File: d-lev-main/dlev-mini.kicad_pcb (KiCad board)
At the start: 4 copper layers, 175.3 x 163.3 mm, 126 parts, among them J1 S12B-PH-SM4-TB, J2 Tag-Connect TC2030-NL, J3 S8B-PH-SM4-TB, J4 S8B-PH-SM4-TB, J5 S6B-PH-SM4-TB, Q1 BSS138, Q2 BSS138, Q3 BSS138, Q4 BSS138, Q5 BSS138, SW1 RotaryEncoder_Switch, SW2 RotaryEncoder_Switch, SW3 RotaryEncoder_Switch, SW4 RotaryEncoder_Switch, SW5 RotaryEncoder_Switch, SW6 RotaryEncoder_Switch, SW7 RotaryEncoder_Switch, SW8 RotaryEncoder_Switch, U2 25LCxxx, U3 AC608, U4 AMS1117-3.3

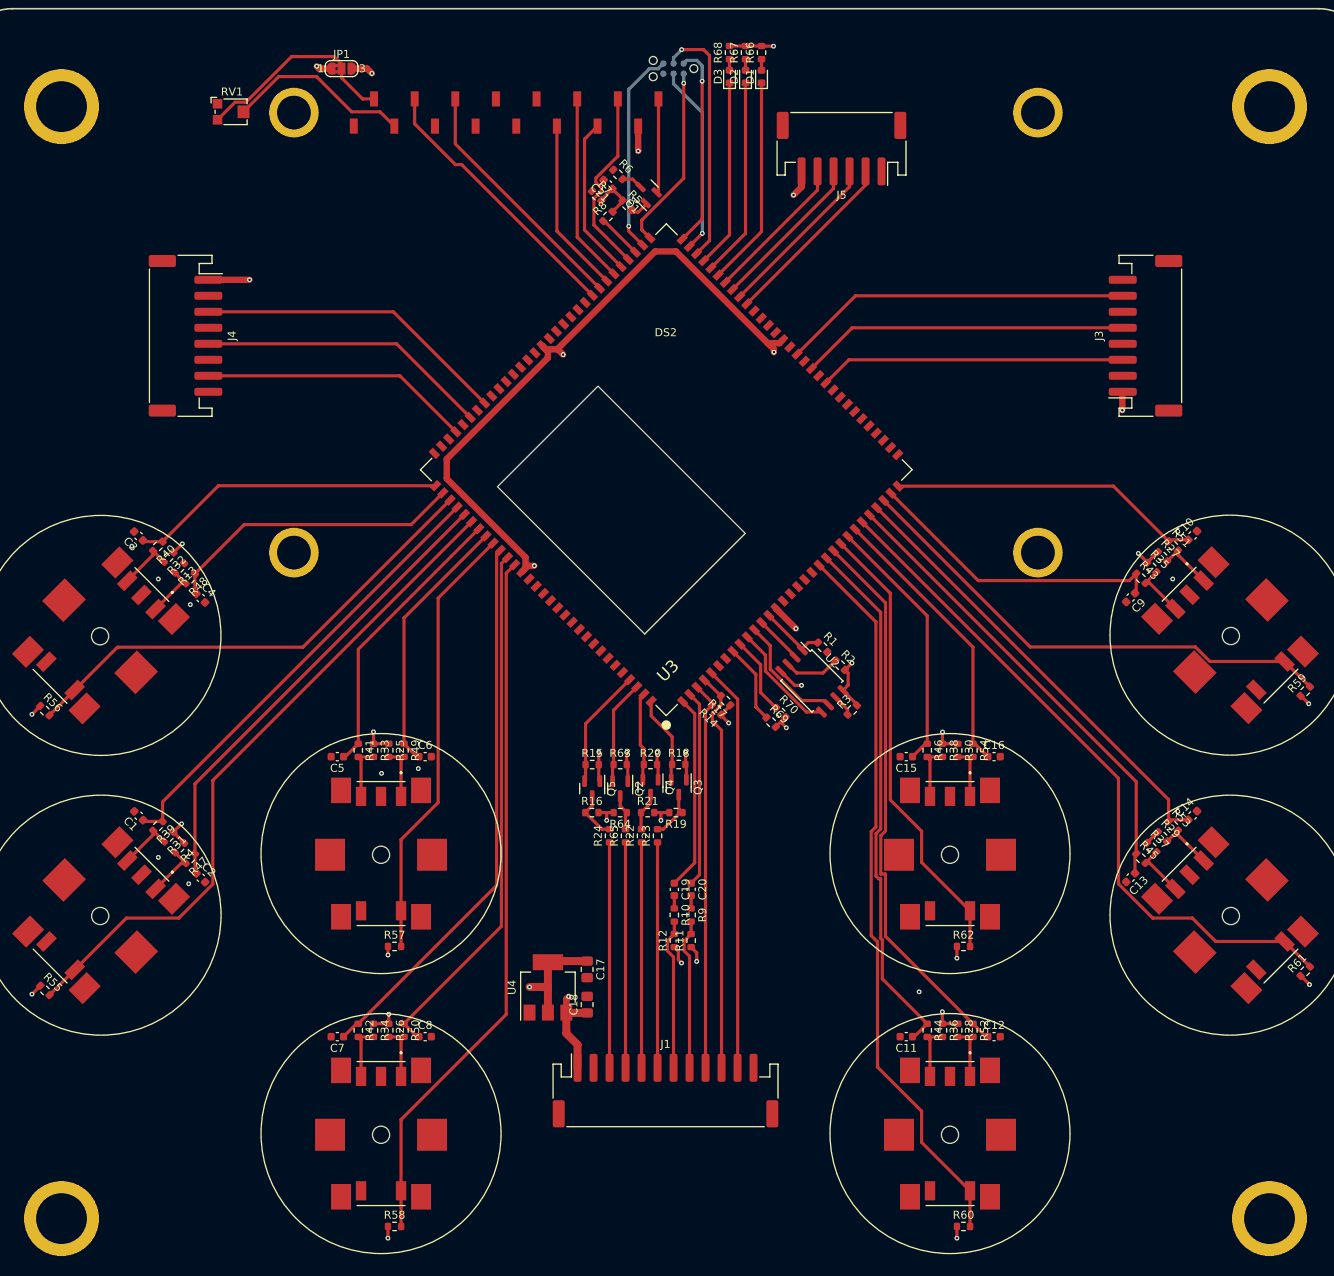
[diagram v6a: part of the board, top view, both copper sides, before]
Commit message: main board - push vias around
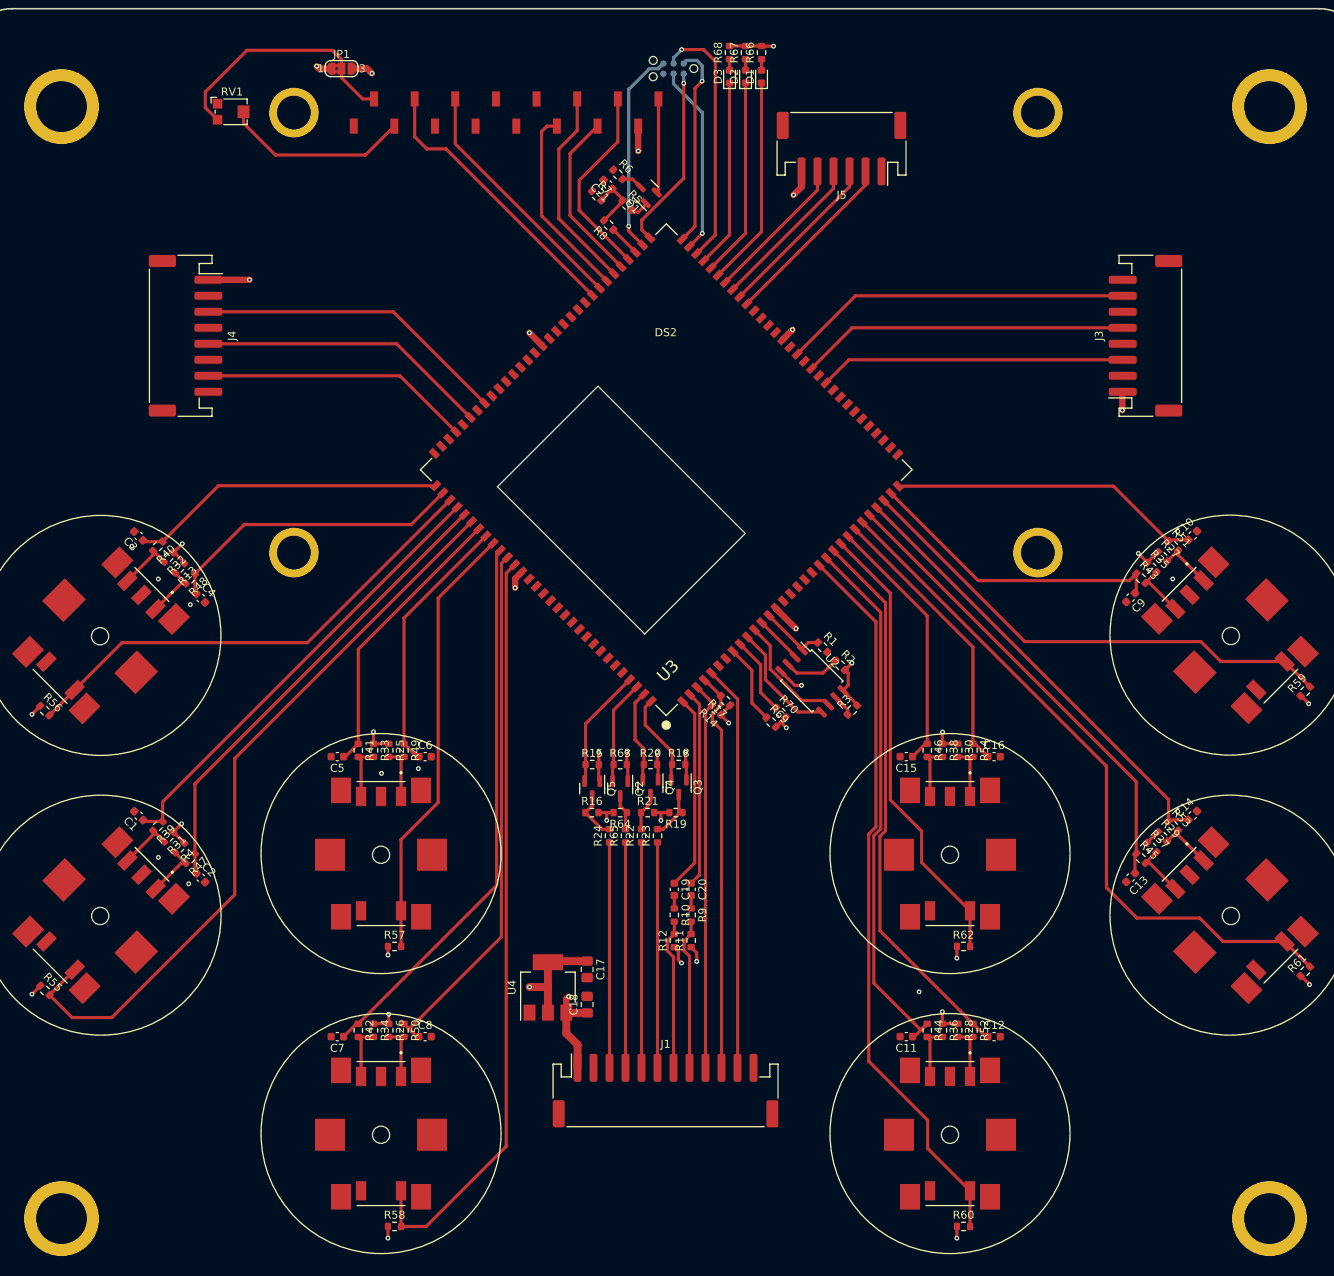
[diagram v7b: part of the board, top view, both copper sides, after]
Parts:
- moved R8 1.08 mm to (-7.11, -83.4), turned to 135 degrees
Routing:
- net +3V3: track 168.9 -> 94.4 mm
- net /FPGA/enc_2.s: track 84.9 -> 94.0 mm
- net /LCD/VLCD: track 26.0 -> 32.4 mm
- net /FPGA/enc_4.s: track 88.6 -> 94.9 mm
- net /FPGA/lcd.data0: track 21.9 -> 24.2 mm
- net /FPGA/lcd.data1: track 23.8 -> 25.7 mm
- net /FPGA/lcd.pwm: track 5.64 -> 3.96 mm
- net /FPGA/enc_8.b: track 66.6 -> 68.3 mm
- net Net-(C21-Pad1): track 5.91 -> 7.43 mm
- net /FPGA/lcd.data2: track 20.1 -> 21.6 mm
- net /FPGA/enc_6.s: track 86.7 -> 87.9 mm
- net /FPGA/lcd.data3: track 23.6 -> 24.6 mm
- net /FPGA/lcd.rs: track 34.2 -> 35.2 mm
- net /FPGA/enc_4.a: track 66.2 -> 66.9 mm
- net /FPGA/mem_spi.di: track 14.3 -> 14.9 mm
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
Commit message: Improve routing and rearrange I/O connector
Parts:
- moved R11 28.8 mm to (-12.0, -18.4), turned to 0 degrees
- moved C20 27.8 mm to (-11.2, -24.2)
- moved R9 27.8 mm to (-11.2, -21.0)
- moved R16 24.0 mm to (7.83, 6.85), turned to 180 degrees
- moved Q5 23.9 mm to (7.83, 3.85)
- moved R15 23.9 mm to (7.73, 0.85)
- moved R24 21.6 mm to (7.84, 8.60), turned to 0 degrees
- moved R64 20.7 mm to (14.8, -13.1), turned to 0 degrees
- moved Q2 20.7 mm to (14.8, -16.1)
- moved R63 20.7 mm to (14.7, -19.1)
- moved R65 20.3 mm to (14.9, -11.3), turned to 180 degrees
- moved R12 16.2 mm to (-6.96, -8.04), turned to 180 degrees
- moved C19 16.1 mm to (-7.76, -13.8)
- moved R10 16.1 mm to (-7.76, -10.6)
- moved R70 16.0 mm to (21.2, -37.0)
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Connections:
- J1 pad 10: mute_btn -> midi_out
- J1 pad 11: mute_led -> GND
- J1 pad 12: GND -> midi_in
- J1 pad 2: GND -> spdif_mon
- J1 pad 3: midi_out -> mute_led
- J1 pad 4: midi_in -> spdif_line
- J1 pad 5: uart_tx_5v -> GND
- J1 pad 6: uart_rx_5v -> uart_tx_5v
- J1 pad 7: spdif_line -> mute_btn
- J1 pad 8: spdif_mon -> uart_rx_5v
- U3 pad 1: /spdif_tx_0 -> /uart_rx_3v
- U3 pad 116: unconnected-(U3-IO_R10-Pad116) -> /spdif_tx_1
- U3 pad 118: unconnected-(U3-IO_R11-Pad118) -> mute_led
- U3 pad 120: /FPGA/midi_tx_n -> /spdif_tx_0
- U3 pad 121: /midi_tx -> unconnected-(U3-IO_T12-Pad121)
- U3 pad 122: /midi_rx -> /uart_tx_3v
- U3 pad 123: /uart_tx_3v -> unconnected-(U3-IO_T13-Pad123)
- U3 pad 124: /uart_rx_3v -> mute_btn
- U3 pad 16: unconnected-(U3-IO_N12-Pad16) -> /FPGA/gpio_o3
- U3 pad 17: unconnected-(U3-IO_P14-Pad17) -> /FPGA/gpio_o2
- U3 pad 18: unconnected-(U3-IO_N14-Pad18) -> /FPGA/gpio_i3
- U3 pad 19: unconnected-(U3-IO_L13-Pad19) -> /FPGA/gpio_i2
- U3 pad 2: /spdif_tx_1 -> unconnected-(U3-IO_T15-Pad2)
- U3 pad 4: mute_btn -> unconnected-(U3-IO_P15-Pad4)
- U3 pad 5: mute_led -> /midi_tx
- U3 pad 6: /FPGA/gpio_o3 -> unconnected-(U3-IO_N15-Pad6)
- U3 pad 7: /FPGA/gpio_o2 -> /midi_rx
- U3 pad 8: /FPGA/gpio_i3 -> unconnected-(U3-I_M15-Pad8)
- U3 pad 9: /FPGA/gpio_i2 -> unconnected-(U3-I_M16-Pad9)
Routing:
- net spdif_mon: track 18.9 -> 50.4 mm
- net spdif_line: track 19.0 -> 40.3 mm
- net +5V: track 297.0 -> 318.2 mm, vias 8 -> 10
- net /midi_tx: track 15.0 -> 35.5 mm
- net /spdif_tx_1: track 24.5 -> 7.05 mm
- net midi_in: track 28.2 -> 42.6 mm
- net uart_tx_5v: track 28.2 -> 41.6 mm
- net uart_rx_5v: track 28.2 -> 41.3 mm
- net acal_btn: track 48.7 -> 59.9 mm
- net +3V3: track 94.4 -> 83.3 mm, vias 29 -> 56
- net /spdif_tx_0: track 24.4 -> 13.6 mm
- net mute_led: track 50.7 -> 60.6 mm
- net /FPGA/enc_2.s: track 94.0 -> 85.8 mm
- net midi_out: track 28.2 -> 20.8 mm
- net /FPGA/gpio_i3: track 10.0 -> 3.63 mm
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- added copper zone on F.Cu, net +3V3
